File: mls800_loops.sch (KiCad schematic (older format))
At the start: 60 parts

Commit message: MLS800  * Lots of change in diagram/schematic  * Added external parts
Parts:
- gave numbers to parts that had none: 60

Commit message: MLS800  * Fixed missing non connected symbols
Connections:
- no-connect marks 0 -> 4

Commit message: MLS800  * Fixed some crc errors  * Fixed wrong AREF/UCAP schematics  * Generated netlist
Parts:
- renumbered Q8 to Q10, Q9 to Q11, Q10 to Q12, Q11 to Q13, Q12 to Q14, Q13 to Q15, Q14 to Q16, Q15 to Q17, Q16 to Q18, Q1 to Q3, Q2 to Q4, Q3 to Q5, Q4 to Q6, Q5 to Q7, Q6 to Q8, Q7 to Q9, R15 to R24, U4 to U5

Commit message: MLS800  * Added separated GND : AGND & GND  * Revamped the loops schema  * Put values on all components  * Started to add footprint annotations to some resistors
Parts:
- removed J10, J11, J12, J13, J14, J15, J16, J17, J18, J19, J2, J3, J4, J5, J6, J7, J8, J9: JACK_2P, ~, symbol JACK_2P
- removed SW2, SW3, SW4, SW5, SW6, SW7, SW8, SW9: LATCH_DPDT, ~, symbol LATCH_DPDT
- added J10, J3, J4, J5, J6, J7, J8, J9: JACK_2P_STACK, ~, symbol JACK_2P_STACK
- added J11, J2: JACK_2P_SW, ~, symbol JACK_2P_SW
- added RE1, RE2, RE3, RE4, RE5, RE6, RE7, RE8: LATCH_DPDT, ~, symbol LATCH_DPDT
- D10, D11, D12, D13, D14, D15, D16, D17, D18, D19, D20, D21, D6, D7, D8, D9: value DIODE -> 1N4148
- Q10, Q11, Q12, Q13, Q14, Q15, Q16, Q17, Q18, Q3, Q4, Q5, Q6, Q7, Q8, Q9: value NPN -> 2N3904
- R24: value R -> 1k
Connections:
- net labels added: AGND, DGND
- net labels removed: GND
- wire segments 194 -> 286

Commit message: MLS800  * Started cmp association
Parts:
- renumbered R24 to R26

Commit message: MLS800 :  - assigning footprints
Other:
- moved on the sheet: D10, D11, D12, D13, D14, D15, D16, D17, D18, D19, D20, D21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

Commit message: MLS800 :  - assigning footprints
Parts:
- D10, D11, D12, D13, D14, D15, D16, D17, D18, D19, D20, D6, D7, D8, D9: footprint ~ -> Imported:SOD-123
- D21: value 1N4148 -> Imported:SOD-123
- U5: footprint MODULE -> Housings_SSOP:SSOP-28
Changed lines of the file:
@@
 F 0 "U5" H 1500 3100 50  0000 C CNN
 F 1 "MCP23017" H 2500 900 50  0000 C CNN
-F 2 "MODULE" H 1550 900 50  0001 C CNN
+F 2 "Housings_SSOP:SSOP-28" H 1550 900 50  0001 C CNN
 F 3 "DOCUMENTATION" H 2050 1950 50  0001 C CNN
 	1    2050 2000
@@
 F 0 "D6" H 4350 1550 40  0000 C CNN
 F 1 "1N4148" H 4350 1350 40  0000 C CNN
-F 2 "~" H 4350 1450 60  0000 C CNN
+F 2 "Imported:SOD-123" H 4350 1450 60  0001 C CNN
 F 3 "~" H 4350 1450 60  0000 C CNN
 	1    4350 1450
@@
 F 0 "D7" H 4350 2100 40  0000 C CNN
 F 1 "1N4148" H 4350 1900 40  0000 C CNN
-F 2 "~" H 4350 2000 60  0000 C CNN
+F 2 "Imported:SOD-123" H 4350 2000 60  0001 C CNN
 F 3 "~" H 4350 2000 60  0000 C CNN
 	1    4350 2000
@@
 F 0 "D8" H 4350 2750 40  0000 C CNN
 F 1 "1N4148" H 4350 2550 40  0000 C CNN
-F 2 "~" H 4350 2650 60  0000 C CNN
+F 2 "Imported:SOD-123" H 4350 2650 60  0001 C CNN
 F 3 "~" H 4350 2650 60  0000 C CNN
 	1    4350 2650
@@
 F 0 "D9" H 4350 3300 40  0000 C CNN
 F 1 "1N4148" H 4350 3100 40  0000 C CNN
-F 2 "~" H 4350 3200 60  0000 C CNN
+F 2 "Imported:SOD-123" H 4350 3200 60  0001 C CNN
 F 3 "~" H 4350 3200 60  0000 C CNN
 	1    4350 3200
@@
 F 0 "D10" H 4350 3950 40  0000 C CNN
 F 1 "1N4148" H 4350 3750 40  0000 C CNN
-F 2 "~" H 4350 3850 60  0000 C CNN
+F 2 "Imported:SOD-123" H 4350 3850 60  0001 C CNN
 F 3 "~" H 4350 3850 60  0000 C CNN
 	1    4350 3850
@@
 F 0 "D11" H 4350 4500 40  0000 C CNN
 F 1 "1N4148" H 4350 4300 40  0000 C CNN
-F 2 "~" H 4350 4400 60  0000 C CNN
+F 2 "Imported:SOD-123" H 4350 4400 60  0001 C CNN
 F 3 "~" H 4350 4400 60  0000 C CNN
 	1    4350 4400
@@
 F 0 "D12" H 4350 5150 40  0000 C CNN
 F 1 "1N4148" H 4350 4950 40  0000 C CNN
-F 2 "~" H 4350 5050 60  0000 C CNN
+F 2 "Imported:SOD-123" H 4350 5050 60  0001 C CNN
 F 3 "~" H 4350 5050 60  0000 C CNN
 	1    4350 5050
@@
 F 0 "D13" H 4350 5700 40  0000 C CNN
 F 1 "1N4148" H 4350 5500 40  0000 C CNN
-F 2 "~" H 4350 5600 60  0000 C CNN
+F 2 "Imported:SOD-123" H 4350 5600 60  0001 C CNN
 F 3 "~" H 4350 5600 60  0000 C CNN
 	1    4350 5600
@@
 F 0 "D14" H 8650 1550 40  0000 C CNN
 F 1 "1N4148" H 8650 1350 40  0000 C CNN
-F 2 "~" H 8650 1450 60  0000 C CNN
+F 2 "Imported:SOD-123" H 8650 1450 60  0001 C CNN
 F 3 "~" H 8650 1450 60  0000 C CNN
 	1    8650 1450
@@
 F 0 "D15" H 8650 2100 40  0000 C CNN
 F 1 "1N4148" H 8650 1900 40  0000 C CNN
-F 2 "~" H 8650 2000 60  0000 C CNN
+F 2 "Imported:SOD-123" H 8650 2000 60  0001 C CNN
 F 3 "~" H 8650 2000 60  0000 C CNN
 	1    8650 2000
@@
 F 0 "D16" H 8650 2750 40  0000 C CNN
 F 1 "1N4148" H 8650 2550 40  0000 C CNN
-F 2 "~" H 8650 2650 60  0000 C CNN
+F 2 "Imported:SOD-123" H 8650 2650 60  0001 C CNN
 F 3 "~" H 8650 2650 60  0000 C CNN
 	1    8650 2650
@@
 F 0 "D17" H 8650 3300 40  0000 C CNN
 F 1 "1N4148" H 8650 3100 40  0000 C CNN
-F 2 "~" H 8650 3200 60  0000 C CNN
+F 2 "Imported:SOD-123" H 8650 3200 60  0001 C CNN
 F 3 "~" H 8650 3200 60  0000 C CNN
 	1    8650 3200
@@
 F 0 "D18" H 8650 3950 40  0000 C CNN
 F 1 "1N4148" H 8650 3750 40  0000 C CNN
-F 2 "~" H 8650 3850 60  0000 C CNN
+F 2 "Imported:SOD-123" H 8650 3850 60  0001 C CNN
 F 3 "~" H 8650 3850 60  0000 C CNN
 	1    8650 3850
@@
 F 0 "D19" H 8650 4500 40  0000 C CNN
 F 1 "1N4148" H 8650 4300 40  0000 C CNN
-F 2 "~" H 8650 4400 60  0000 C CNN
+F 2 "Imported:SOD-123" H 8650 4400 60  0001 C CNN
 F 3 "~" H 8650 4400 60  0000 C CNN
 	1    8650 4400
@@
 F 0 "D20" H 8650 5150 40  0000 C CNN
 F 1 "1N4148" H 8650 4950 40  0000 C CNN
-F 2 "~" H 8650 5050 60  0000 C CNN
+F 2 "Imported:SOD-123" H 8650 5050 60  0001 C CNN
 F 3 "~" H 8650 5050 60  0000 C CNN
 	1    8650 5050
@@
 P 8650 5600
 F 0 "D21" H 8650 5700 40  0000 C CNN
-F 1 "1N4148" H 8650 5500 40  0000 C CNN
+F 1 "Imported:SOD-123" H 8650 5500 40  0001 C CNN
 F 2 "~" H 8650 5600 60  0000 C CNN
 F 3 "~" H 8650 5600 60  0000 C CNN
@@
 	7800 1350 7800 6100
 Wire Bus Line
-	3500 6100 7800 6100
+	7800 6100 3500 6100
 Wire Bus Line
-	3500 1200 3500 6100
+	3500 6100 3500 1200
 $Comp
 L DGND #PWR0102
@@
 	9500 3700 9500 3250
 Wire Bus Line
-	3200 1200 3500 1200
+	3500 1200 3200 1200
 $EndSCHEMATC

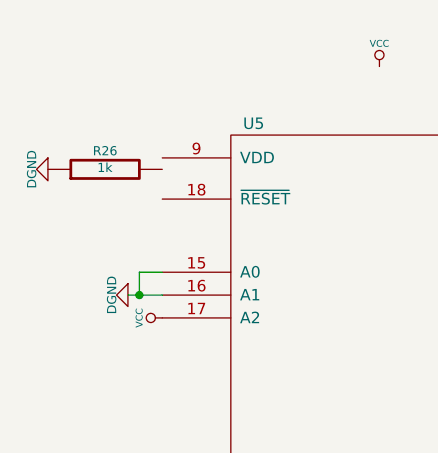
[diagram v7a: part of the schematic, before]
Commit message: MLS800 : created custom librairies
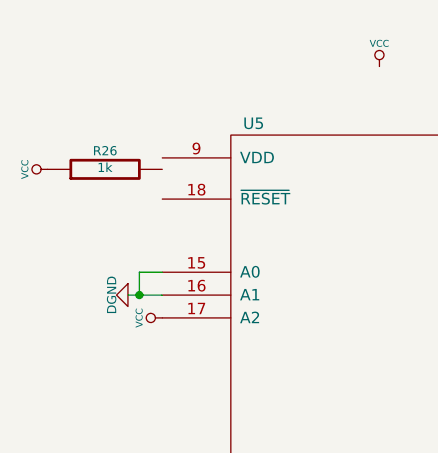
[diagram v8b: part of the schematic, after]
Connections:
- net DGND: no longer R26.1
- net VCC: now also R26.1
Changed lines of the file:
@@
 LIBS:contrib
 LIBS:valves
+LIBS:custom-i2c
+LIBS:custom-opto
+LIBS:custom-conn
+LIBS:custom-device
 LIBS:mls800-cache
 EELAYER 24 0
@@
 $Descr A4 11693 8268
 encoding utf-8
-Sheet 4 4
+Sheet 4 5
 Title "noname.sch"
 Date "18 aug 2014"
@@
 	1    0    0    -1
 $EndComp
-$Comp
-L DGND #PWR0103
-U 1 1 53F19FB3
+Wire Wire Line
+	5200 3700 5200 3250
+Wire Wire Line
+	9500 3700 9500 3250
+Wire Bus Line
+	3500 1200 3200 1200
+$Comp
+L VCC #PWR?
+U 1 1 543C6A1E
 P 600 1100
-F 0 "#PWR0103" H 600 1100 40  0001 C CNN
-F 1 "DGND" H 600 1030 40  0000 C CNN
+F 0 "#PWR?" H 600 1200 30  0001 C CNN
+F 1 "VCC" H 600 1200 30  0000 C CNN
 F 2 "" H 600 1100 60  0000 C CNN
 F 3 "" H 600 1100 60  0000 C CNN
 	1    600  1100
-	0    1    1    0
-$EndComp
-Wire Wire Line
-	5200 3700 5200 3250
-Wire Wire Line
-	9500 3700 9500 3250
-Wire Bus Line
-	3500 1200 3200 1200
+	0    -1   -1   0
+$EndComp
 $EndSCHEMATC
